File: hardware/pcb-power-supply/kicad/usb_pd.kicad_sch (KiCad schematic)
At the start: 12 parts, among them U1 STUSB4500LQTR, U2 USBLC6-2SC6

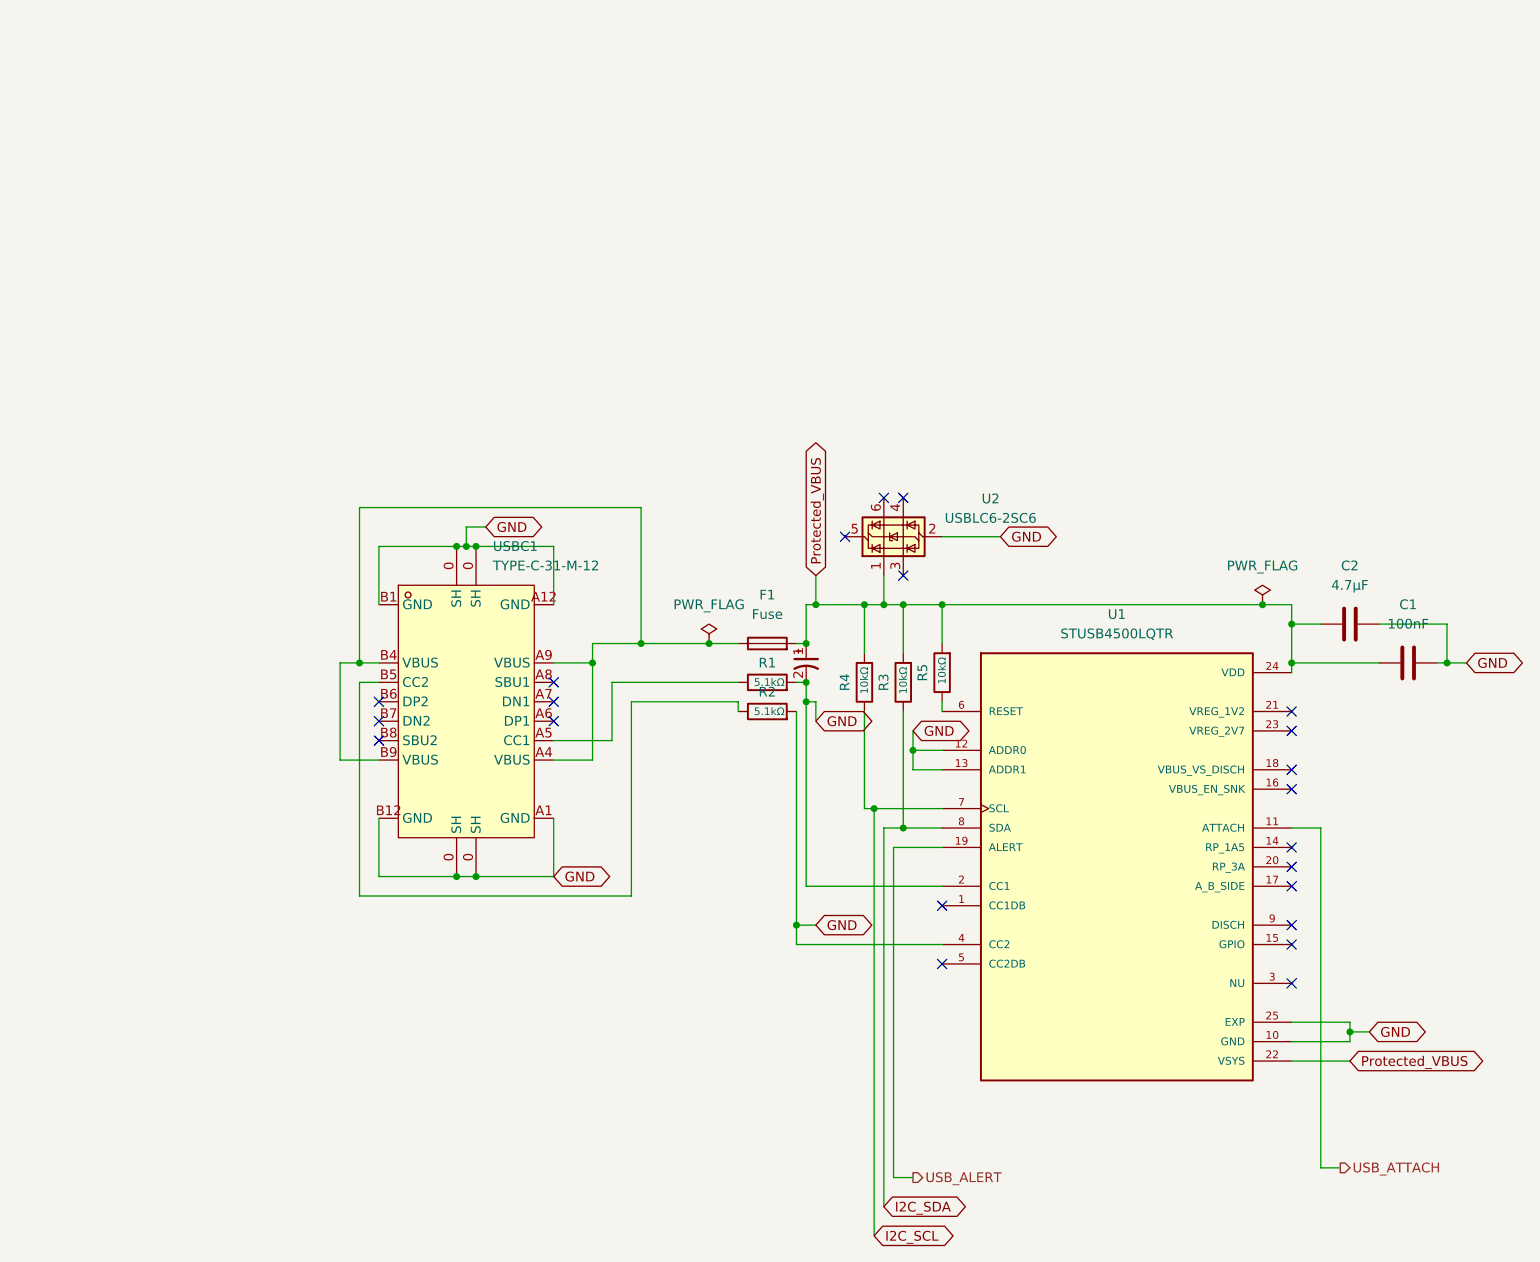
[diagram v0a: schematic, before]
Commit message: Add circuit-context.json for power supply PCB
Extract and annotate schematic context for the power supply board
(50 components, 29 nets, 4 functional blocks across 5 sheets).
Covers USB PD negotiation (STUSB4500), battery management (BQ24195),
power distribution (MT3608 boost + LR1801 LDO), and output connectors.

Creates power-schematic-context initiative docs (BRIEF/PLAN/TASKS).
Component ai_ annotations written to .kicad_sch files via annotate.py;
net/block annotations stored in circuit-context.json.

Made-with: Cursor
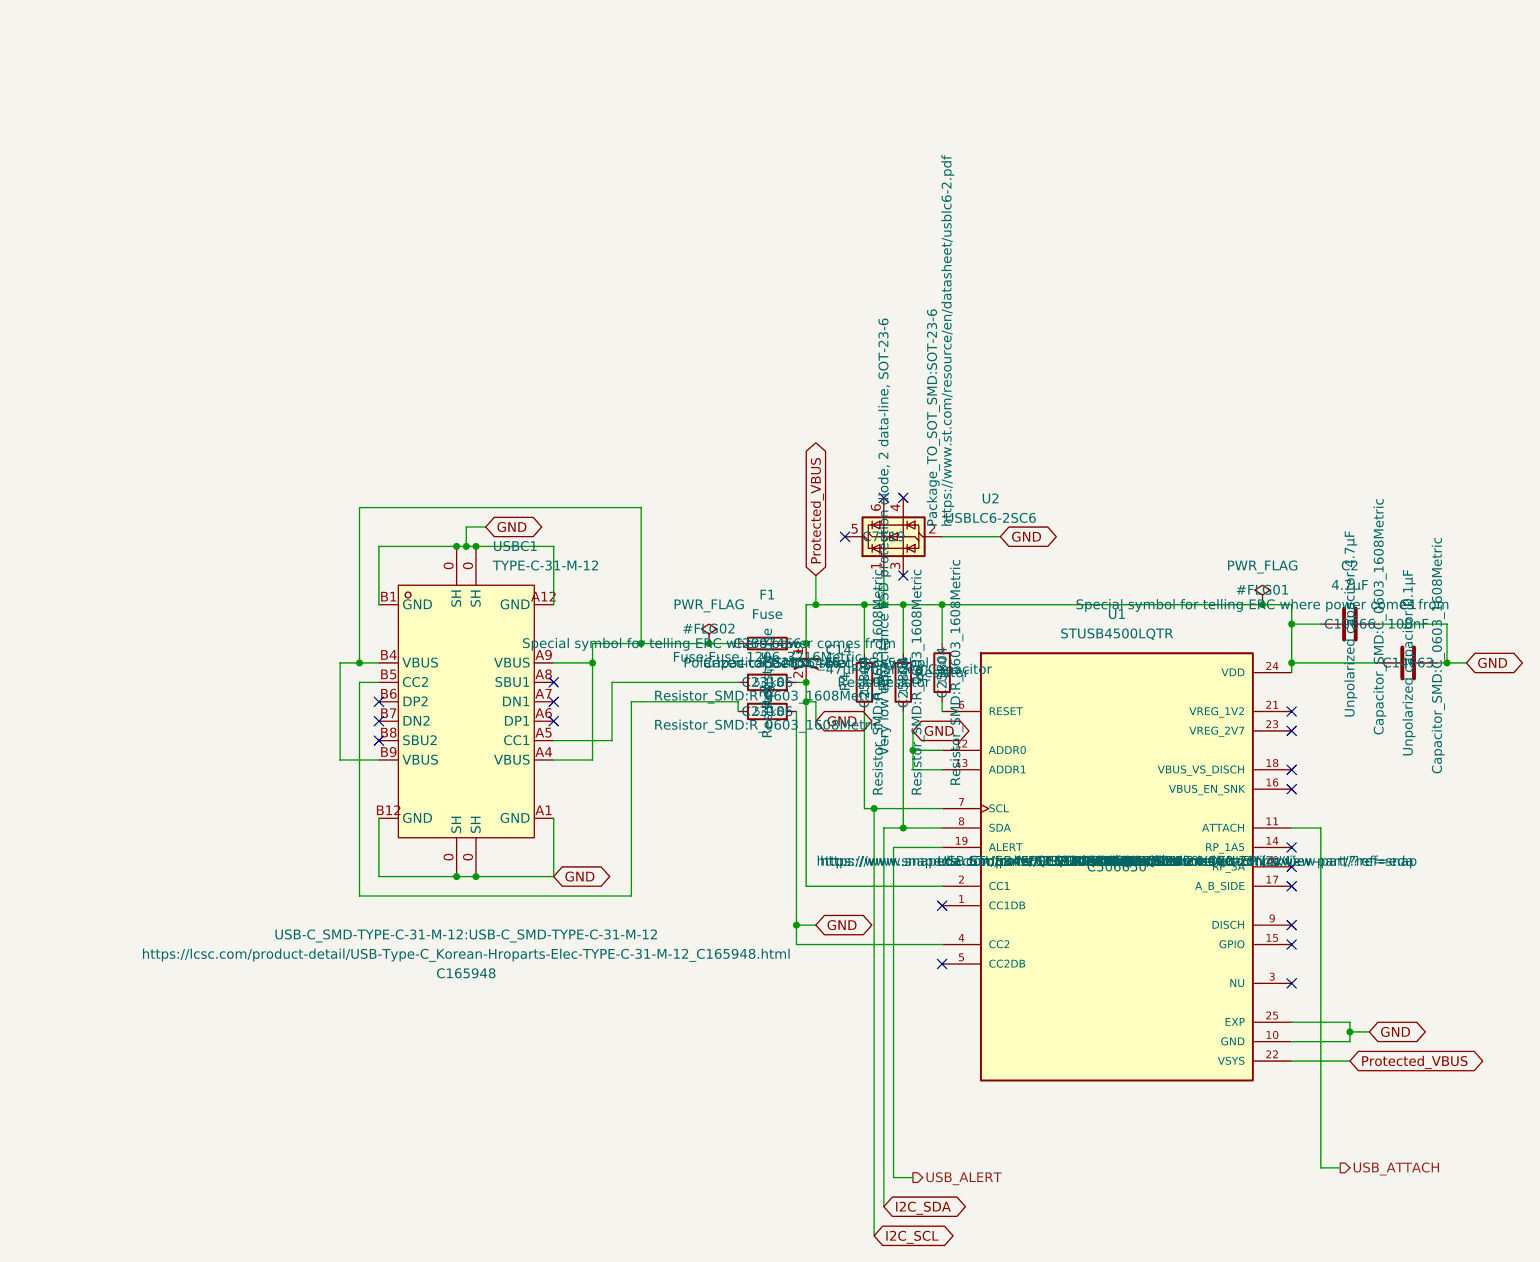
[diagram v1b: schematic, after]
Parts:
- C1: ai_block (none) -> usb_pd; ai_critical_specs (none) -> 100nF ceramic; ai_function (none) -> STUSB4500 VDD bypass capacitor; ai_role (none) -> bypass
- C14: ai_block (none) -> usb_pd; ai_critical_specs (none) -> 47uF electrolytic; ai_function (none) -> Protected_VBUS bulk decoupling capacitor; ai_role (none) -> bulk_decoupling
- C2: ai_block (none) -> usb_pd; ai_critical_specs (none) -> 4.7uF ceramic; ai_function (none) -> Protected_VBUS decoupling capacitor; ai_role (none) -> decoupling
- F1: ai_block (none) -> usb_pd; ai_critical_specs (none) -> 1206 package; ai_function (none) -> VBUS input fuse for overcurrent protection; ai_role (none) -> protection
- R1: ai_block (none) -> usb_pd; ai_critical_specs (none) -> 5.1k per USB-C spec; ai_function (none) -> CC1 pull-down for UFP sink detection; ai_role (none) -> pull_down
- R2: ai_block (none) -> usb_pd; ai_critical_specs (none) -> 5.1k per USB-C spec; ai_function (none) -> CC2 pull-down for UFP sink detection; ai_role (none) -> pull_down
- R3: ai_block (none) -> usb_pd; ai_critical_specs (none) -> 10k; ai_function (none) -> I2C SDA pull-up to Protected_VBUS; ai_role (none) -> pull_up
- R4: ai_block (none) -> usb_pd; ai_critical_specs (none) -> 10k; ai_function (none) -> I2C SCL pull-up to Protected_VBUS; ai_role (none) -> pull_up
- R5: ai_block (none) -> usb_pd; ai_critical_specs (none) -> 10k; ai_function (none) -> STUSB4500 RESET pull-up, active-low held inactive; ai_role (none) -> pull_up
- U1: ai_block (none) -> usb_pd; ai_critical_specs (none) -> I2C configurable, ADDR 0x28; ai_function (none) -> USB PD controller, negotiates voltage and current with USB 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; ai_role (none) -> pd_controller
- U2: ai_block (none) -> usb_pd; ai_critical_specs (none) -> Low capacitance SOT-23-6; ai_function (none) -> USB ESD protection for data lines; ai_role (none) -> esd_protection
- USBC1: ai_block (none) -> usb_pd; ai_function (none) -> USB Type-C power input connector; ai_role (none) -> connector
